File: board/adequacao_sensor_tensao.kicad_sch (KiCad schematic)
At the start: 6 parts, among them J2 Conn_01x02_Pin, U3 LV25-P

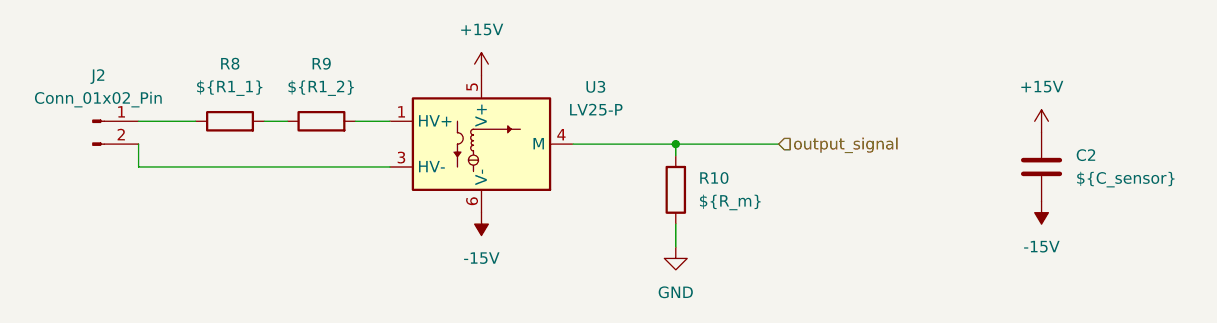
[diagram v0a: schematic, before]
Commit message: Finalização da placa, trilhas, planos de terra e footprint TJA1050
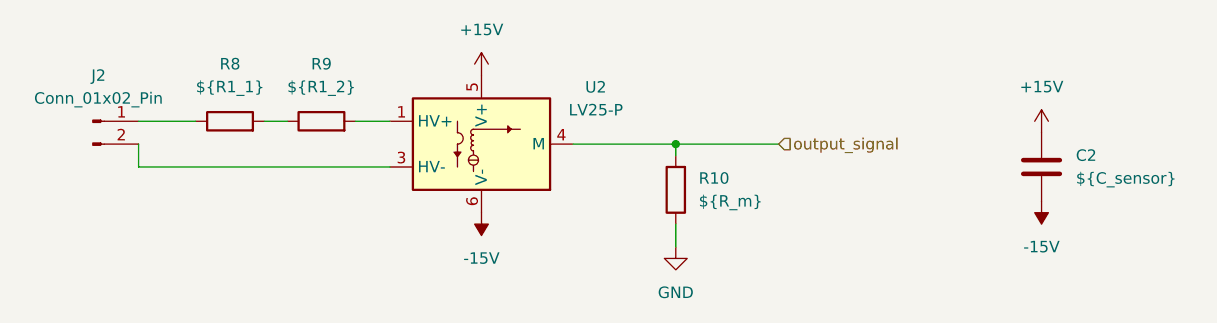
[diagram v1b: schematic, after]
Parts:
- renumbered U3 to U2
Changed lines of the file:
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@@
 		(dnp no)
 		(fields_autoplaced yes)
-		(property "Reference" "#PWR27"
+		(property "Reference" "#PWR24"
 			(at 161.29 74.93 0)
 			(effects
@@
 			(project "board"
 				(path "/d7be55ed-3561-4de6-aa99-76e883d44fb9/484b45ac-854b-4808-a94a-82052b89ba4d/9701d4b2-9f70-4dc2-8f65-3cb2cc418c7b"
-					(reference "#PWR27")
-					(unit 1)
-				)
-				(path "/d7be55ed-3561-4de6-aa99-76e883d44fb9/484b45ac-854b-4808-a94a-82052b89ba4d/d6523acf-4a35-49b3-8df2-392463f7dfc0"
-					(reference "#PWR32")
+					(reference "#PWR24")
+					(unit 1)
+				)
+				(path "/d7be55ed-3561-4de6-aa99-76e883d44fb9/484b45ac-854b-4808-a94a-82052b89ba4d/d6523acf-4a35-49b3-8df2-392463f7dfc0"
+					(reference "#PWR29")
 					(unit 1)
 				)
@@
 		(dnp no)
 		(fields_autoplaced yes)
-		(property "Reference" "U3"
+		(property "Reference" "U2"
 			(at 111.76 66.0714 0)
 			(effects
@@
 			(project "board"
 				(path "/d7be55ed-3561-4de6-aa99-76e883d44fb9/484b45ac-854b-4808-a94a-82052b89ba4d/9701d4b2-9f70-4dc2-8f65-3cb2cc418c7b"
+					(reference "U2")
+					(unit 1)
+				)
+				(path "/d7be55ed-3561-4de6-aa99-76e883d44fb9/484b45ac-854b-4808-a94a-82052b89ba4d/d6523acf-4a35-49b3-8df2-392463f7dfc0"
 					(reference "U3")
-					(unit 1)
-				)
-				(path "/d7be55ed-3561-4de6-aa99-76e883d44fb9/484b45ac-854b-4808-a94a-82052b89ba4d/d6523acf-4a35-49b3-8df2-392463f7dfc0"
-					(reference "U4")
 					(unit 1)
 				)
@@
 		(dnp no)
 		(fields_autoplaced yes)
-		(property "Reference" "#PWR24"
+		(property "Reference" "#PWR21"
 			(at 99.06 68.58 0)
 			(effects
@@
 			(project "board"
 				(path "/d7be55ed-3561-4de6-aa99-76e883d44fb9/484b45ac-854b-4808-a94a-82052b89ba4d/9701d4b2-9f70-4dc2-8f65-3cb2cc418c7b"
-					(reference "#PWR24")
-					(unit 1)
-				)
-				(path "/d7be55ed-3561-4de6-aa99-76e883d44fb9/484b45ac-854b-4808-a94a-82052b89ba4d/d6523acf-4a35-49b3-8df2-392463f7dfc0"
-					(reference "#PWR29")
+					(reference "#PWR21")
+					(unit 1)
+				)
+				(path "/d7be55ed-3561-4de6-aa99-76e883d44fb9/484b45ac-854b-4808-a94a-82052b89ba4d/d6523acf-4a35-49b3-8df2-392463f7dfc0"
+					(reference "#PWR26")
 					(unit 1)
 				)
@@
 		(dnp no)
 		(fields_autoplaced yes)
-		(property "Reference" "#PWR25"
+		(property "Reference" "#PWR22"
 			(at 99.06 76.2 0)
 			(effects
@@
 			(project "board"
 				(path "/d7be55ed-3561-4de6-aa99-76e883d44fb9/484b45ac-854b-4808-a94a-82052b89ba4d/9701d4b2-9f70-4dc2-8f65-3cb2cc418c7b"
-					(reference "#PWR25")
-					(unit 1)
-				)
-				(path "/d7be55ed-3561-4de6-aa99-76e883d44fb9/484b45ac-854b-4808-a94a-82052b89ba4d/d6523acf-4a35-49b3-8df2-392463f7dfc0"
-					(reference "#PWR30")
+					(reference "#PWR22")
+					(unit 1)
+				)
+				(path "/d7be55ed-3561-4de6-aa99-76e883d44fb9/484b45ac-854b-4808-a94a-82052b89ba4d/d6523acf-4a35-49b3-8df2-392463f7dfc0"
+					(reference "#PWR27")
 					(unit 1)
 				)
@@
 		(dnp no)
 		(fields_autoplaced yes)
-		(property "Reference" "#PWR26"
+		(property "Reference" "#PWR23"
 			(at 120.65 90.17 0)
 			(effects
@@
 			(project "board"
 				(path "/d7be55ed-3561-4de6-aa99-76e883d44fb9/484b45ac-854b-4808-a94a-82052b89ba4d/9701d4b2-9f70-4dc2-8f65-3cb2cc418c7b"
-					(reference "#PWR26")
-					(unit 1)
-				)
-				(path "/d7be55ed-3561-4de6-aa99-76e883d44fb9/484b45ac-854b-4808-a94a-82052b89ba4d/d6523acf-4a35-49b3-8df2-392463f7dfc0"
-					(reference "#PWR31")
+					(reference "#PWR23")
+					(unit 1)
+				)
+				(path "/d7be55ed-3561-4de6-aa99-76e883d44fb9/484b45ac-854b-4808-a94a-82052b89ba4d/d6523acf-4a35-49b3-8df2-392463f7dfc0"
+					(reference "#PWR28")
 					(unit 1)
 				)
@@
 		(dnp no)
 		(fields_autoplaced yes)
-		(property "Reference" "#PWR28"
+		(property "Reference" "#PWR25"
 			(at 161.29 74.93 0)
 			(effects
@@
 			(project "board"
 				(path "/d7be55ed-3561-4de6-aa99-76e883d44fb9/484b45ac-854b-4808-a94a-82052b89ba4d/9701d4b2-9f70-4dc2-8f65-3cb2cc418c7b"
-					(reference "#PWR28")
-					(unit 1)
-				)
-				(path "/d7be55ed-3561-4de6-aa99-76e883d44fb9/484b45ac-854b-4808-a94a-82052b89ba4d/d6523acf-4a35-49b3-8df2-392463f7dfc0"
-					(reference "#PWR33")
-					(unit 1)
-				)
+					(reference "#PWR25")
+					(unit 1)
+				)
+				(path "/d7be55ed-3561-4de6-aa99-76e883d44fb9/484b45ac-854b-4808-a94a-82052b89ba4d/d6523acf-4a35-49b3-8df2-392463f7dfc0"
+					(reference "#PWR30")
+					(unit 1)
+				)

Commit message: Criação da placa de alimentação
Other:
- company: (none) -> Escola Politécnica da Universidade de São Paulo
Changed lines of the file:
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@@
 	(generator_version "8.0")
 	(paper "A4")
+	(title_block
+		(date "2025-10-02")
+		(company "Escola Politécnica da Universidade de São Paulo")
+	)
 	(junction
 		(at 120.65 72.39)
